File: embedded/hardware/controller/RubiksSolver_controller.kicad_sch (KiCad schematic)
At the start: 3 parts

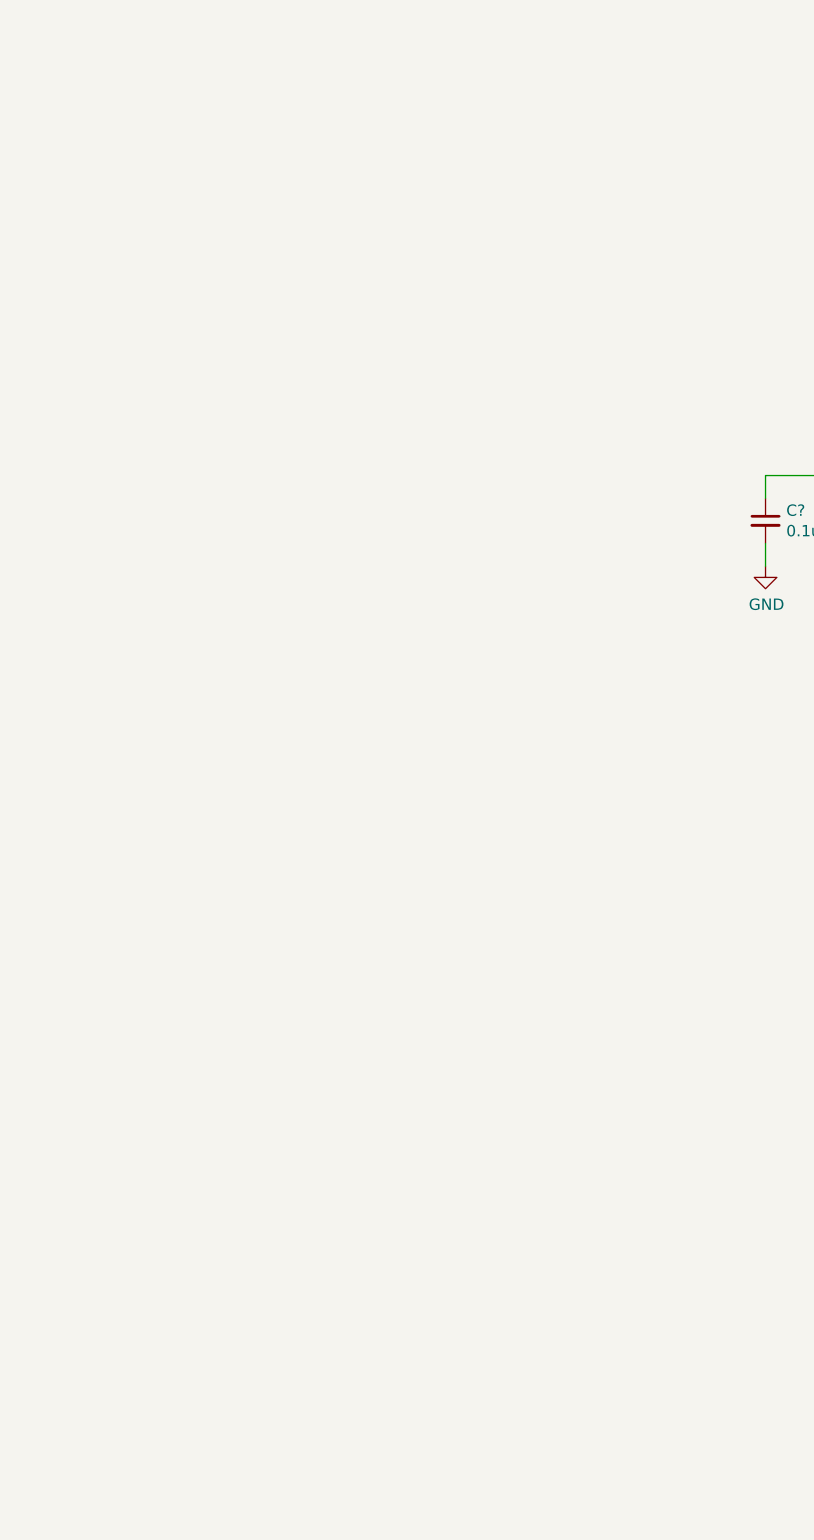
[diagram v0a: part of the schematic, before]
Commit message: Add USB Type-C receptacle
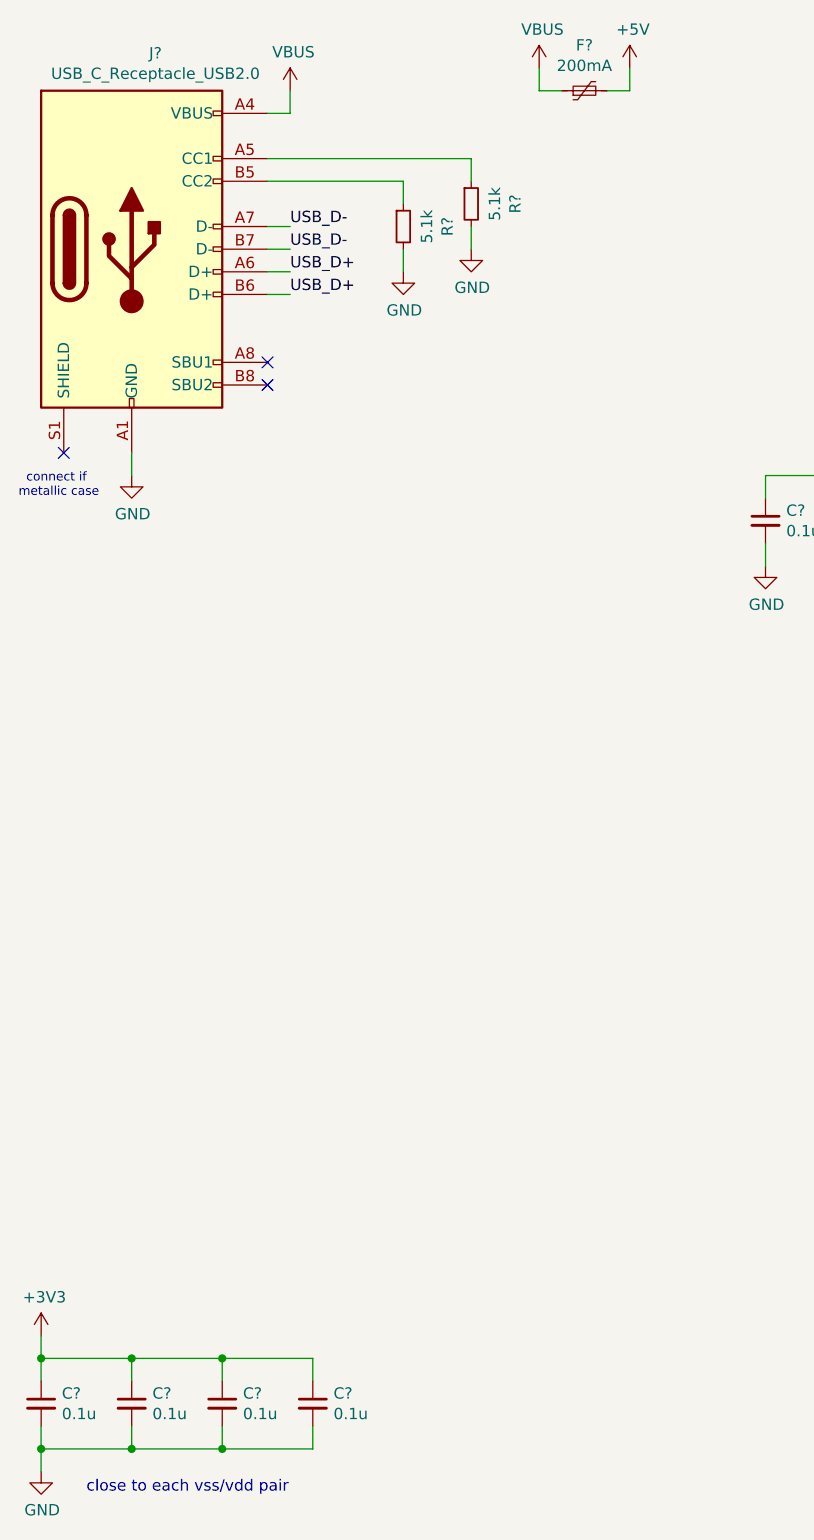
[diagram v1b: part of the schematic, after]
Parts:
- added C? (x4): 0.1u, symbol Device:C_Small
- added F?: 200mA, symbol Device:Polyfuse_Small
- added J?: USB_C_Receptacle_USB2.0, User:USB_C_Receptacle_HRO_TYPE-C-31-M-12, symbol User:USB_C_Receptacle_USB2.0
- added R? (x2): 5.1k, symbol Device:R_Small
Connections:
- net +3V3: now also C?.1, C?.1, C?.1, C?.1
- net GND: now also C?.2, C?.2, C?.2, C?.2, J?.A1 (GND), J?.A12 (GND), J?.B1 (GND), J?.B12 (GND), R?.2, R?.2
- new net: J?.A5 (CC1), R?.1
- new net: J?.B5 (CC2), R?.1
- new net +5V: F?.2
- new net USB_D+: J?.A6 (D+), J?.B6 (D+)
- new net USB_D-: J?.A7 (D-), J?.B7 (D-)
- new net VBUS: F?.1, J?.A4 (VBUS), J?.A9 (VBUS), J?.B4 (VBUS), J?.B9 (VBUS)
- no-connect marks 0 -> 3
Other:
- note added: "close to each vss/vdd pair"
- note added: "connect if metallic case"

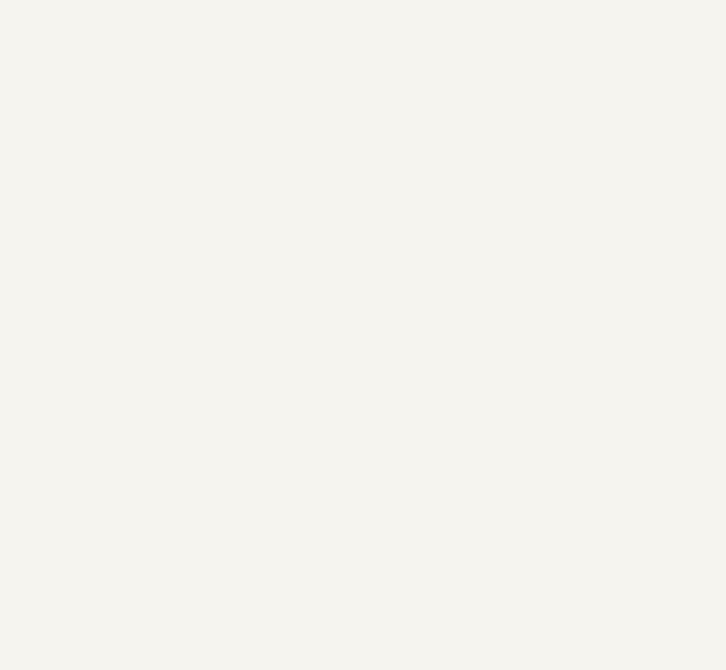
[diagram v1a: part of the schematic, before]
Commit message: Add 10pin programming header
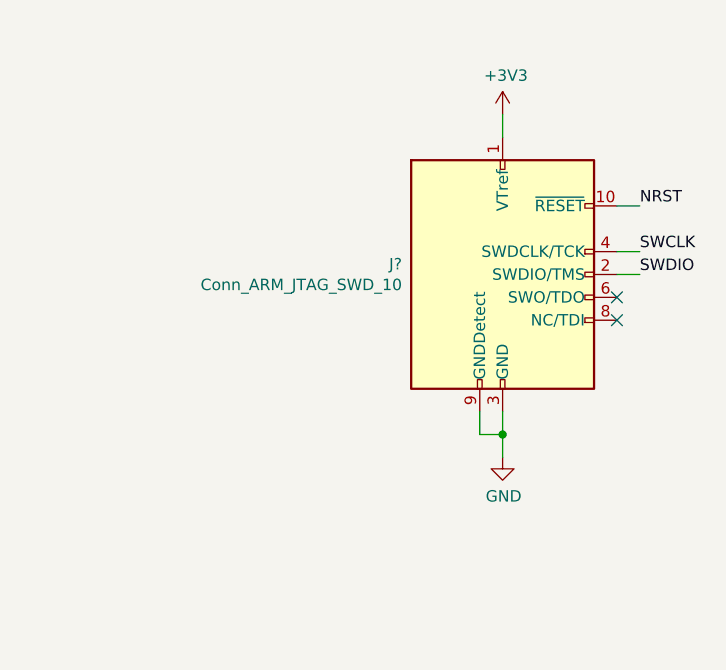
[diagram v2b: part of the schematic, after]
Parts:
- added J?: Conn_ARM_JTAG_SWD_10, symbol Connector:Conn_ARM_JTAG_SWD_10
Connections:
- net +3V3: now also J?.1 (VTref)
- net GND: now also J?.3 (GND), J?.5 (GND), J?.9 (GNDDetect)
- new net NRST: J?.10 (~RESET~)
- new net SWCLK: J?.4 (SWDCLK/TCK)
- new net SWDIO: J?.2 (SWDIO/TMS)
- no-connect marks 3 -> 5
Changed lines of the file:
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@@
   (junction (at 152.4 142.24) (diameter 0.9144) (color 0 0 0 0))
   (junction (at 154.94 60.96) (diameter 0.9144) (color 0 0 0 0))
+  (junction (at 241.3 63.5) (diameter 0.9144) (color 0 0 0 0))
   (no_connect (at 60.96 55.88))
   (no_connect (at 60.96 58.42))
+  (no_connect (at 254 48.26))
   (no_connect (at 38.1 66.04))
+  (no_connect (at 254 50.8))
   (wire (pts (xy 35.56 165.1) (xy 35.56 167.64))
     (stroke (width 0) (type solid) (color 0 0 0 0))
@@
   )
   (wire (pts (xy 157.48 60.96) (xy 157.48 63.5))
+    (stroke (width 0) (type solid) (color 0 0 0 0))
+  )
+  (wire (pts (xy 238.76 60.96) (xy 238.76 63.5))
+    (stroke (width 0) (type solid) (color 0 0 0 0))
+  )
+  (wire (pts (xy 238.76 63.5) (xy 241.3 63.5))
+    (stroke (width 0) (type solid) (color 0 0 0 0))
+  )
+  (wire (pts (xy 241.3 27.94) (xy 241.3 30.48))
+    (stroke (width 0) (type solid) (color 0 0 0 0))
+  )
+  (wire (pts (xy 241.3 60.96) (xy 241.3 63.5))
+    (stroke (width 0) (type solid) (color 0 0 0 0))
+  )
+  (wire (pts (xy 241.3 63.5) (xy 241.3 66.04))
+    (stroke (width 0) (type solid) (color 0 0 0 0))
+  )
+  (wire (pts (xy 254 38.1) (xy 256.54 38.1))
+    (stroke (width 0) (type solid) (color 0 0 0 0))
+  )
+  (wire (pts (xy 254 43.18) (xy 256.54 43.18))
+    (stroke (width 0) (type solid) (color 0 0 0 0))
+  )
+  (wire (pts (xy 254 45.72) (xy 256.54 45.72))
     (stroke (width 0) (type solid) (color 0 0 0 0))
   )
@@
     (effects (font (size 1.27 1.27)) (justify left bottom))
   )
+  (label "NRST" (at 256.54 38.1 0)
+    (effects (font (size 1.27 1.27)) (justify left bottom))
+  )
+  (label "SWCLK" (at 256.54 43.18 0)
+    (effects (font (size 1.27 1.27)) (justify left bottom))
+  )
+  (label "SWDIO" (at 256.54 45.72 0)
+    (effects (font (size 1.27 1.27)) (justify left bottom))
+  )
   (symbol (lib_id "power:+3V3") (at 35.56 165.1 0) (unit 1)
     (in_bom yes) (on_board yes)
@@
     )
   )
+  (symbol (lib_id "power:+3V3") (at 241.3 27.94 0) (unit 1)
+    (in_bom yes) (on_board yes)
+    (property "Reference" "#PWR?" (id 0) (at 241.3 31.75 0)
+      (effects (font (size 1.27 1.27)) hide)
+    )
+    (property "Value" "+3V3" (id 1) (at 241.6683 23.6156 0))
+    (property "Footprint" "" (id 2) (at 241.3 27.94 0)
+      (effects (font (size 1.27 1.27)) hide)
+    )
+    (property "Datasheet" "" (id 3) (at 241.3 27.94 0)
+      (effects (font (size 1.27 1.27)) hide)
+    )
+  )
   (symbol (lib_id "power:GND") (at 35.56 180.34 0) (unit 1)
     (in_bom yes) (on_board yes)
@@
     )
     (property "Datasheet" "" (id 3) (at 147.32 144.78 0)
+      (effects (font (size 1.27 1.27)) hide)
+    )
+  )
+  (symbol (lib_id "power:GND") (at 241.3 66.04 0) (unit 1)
+    (in_bom yes) (on_board yes)
+    (property "Reference" "#PWR?" (id 0) (at 241.3 72.39 0)
+      (effects (font (size 1.27 1.27)) hide)
+    )
+    (property "Value" "GND" (id 1) (at 241.4143 70.3644 0))
+    (property "Footprint" "" (id 2) (at 241.3 66.04 0)
+      (effects (font (size 1.27 1.27)) hide)
+    )
+    (property "Datasheet" "" (id 3) (at 241.3 66.04 0)
       (effects (font (size 1.27 1.27)) hide)
     )
@@
     )
   )
+  (symbol (lib_id "Connector:Conn_ARM_JTAG_SWD_10") (at 241.3 45.72 0) (unit 1)
+    (in_bom yes) (on_board yes)
+    (property "Reference" "J?" (id 0) (at 230.1239 44.5706 0)
+      (effects (font (size 1.27 1.27)) (justify right))
+    )
+    (property "Value" "Conn_ARM_JTAG_SWD_10" (id 1) (at 230.1239 46.8693 0)
+      (effects (font (size 1.27 1.27)) (justify right))
+    )
+    (property "Footprint" "" (id 2) (at 241.3 45.72 0)
+      (effects (font (size 1.27 1.27)) hide)
+    )
+    (property "Datasheet" "http://infocenter.arm.com/help/topic/com.arm.doc.ddi0314h/DDI0314H_coresight_components_trm.pdf" (id 3) (at 232.41 77.47 90)
+      (effects (font (size 1.27 1.27)) hide)
+    )
+  )
   (symbol (lib_id "User:USB_C_Receptacle_USB2.0") (at 45.72 43.18 0) (unit 1)
     (in_bom yes) (on_board yes)
@@
   )
   (symbol_instances
+    (path "/259b77ed-a074-4b54-8027-04ba979215be"
+      (reference "#PWR?") (unit 1) (value "GND") (footprint "")
+    )
     (path "/2a143cb8-a1de-4742-8f35-f2f7b31e5171"
       (reference "#PWR?") (unit 1) (value "GND") (footprint "")
@@
       (reference "#PWR?") (unit 1) (value "+5V") (footprint "")
     )
+    (path "/6128e785-f6ee-489b-8337-ca8a83111c1b"
+      (reference "#PWR?") (unit 1) (value "+3V3") (footprint "")
+    )
     (path "/64c8ed70-14a8-4a73-98d8-e686a93ff02b"
       (reference "#PWR?") (unit 1) (value "+3V3") (footprint "")
@@
       (reference "F?") (unit 1) (value "200mA") (footprint "")
     )
+    (path "/1b09b775-5ad9-4d5e-b556-9eea678e2fda"
+      (reference "J?") (unit 1) (value "Conn_ARM_JTAG_SWD_10") (footprint "")
+    )
     (path "/21b2b0fd-3066-40b4-9516-728461709173"

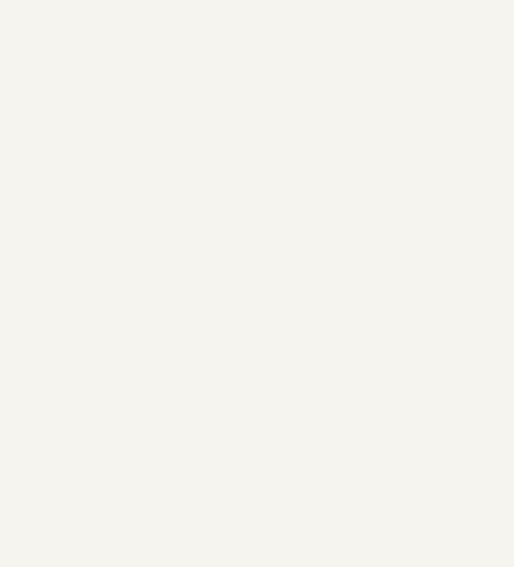
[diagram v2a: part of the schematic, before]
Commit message: Add 4x mounting holes
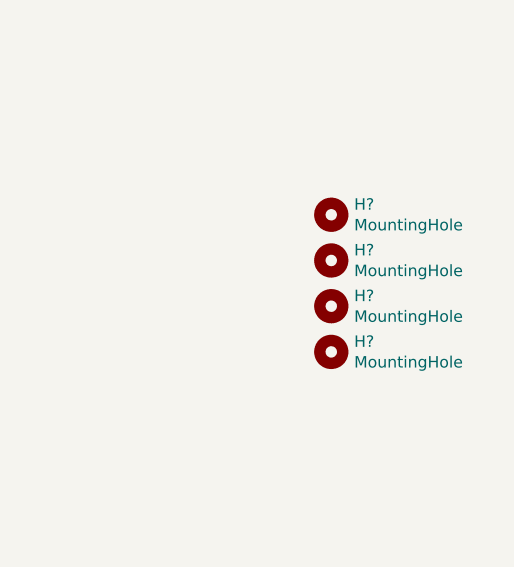
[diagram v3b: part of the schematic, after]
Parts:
- added H? (x4): MountingHole, symbol Mechanical:MountingHole
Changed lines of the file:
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@@
+    )
+  )
+  (symbol (lib_id "Mechanical:MountingHole") (at 256.54 139.7 0) (unit 1)
+    (in_bom yes) (on_board yes)
+    (property "Reference" "H?" (id 0) (at 259.0801 138.5506 0)
+      (effects (font (size 1.27 1.27)) (justify left))
+    )
+    (property "Value" "MountingHole" (id 1) (at 259.0801 140.8493 0)
+      (effects (font (size 1.27 1.27)) (justify left))
+    )
+    (property "Footprint" "" (id 2) (at 256.54 139.7 0)
+      (effects (font (size 1.27 1.27)) hide)
+    )
+    (property "Datasheet" "~" (id 3) (at 256.54 139.7 0)
+      (effects (font (size 1.27 1.27)) hide)
+    )
+  )
+  (symbol (lib_id "Mechanical:MountingHole") (at 256.54 144.78 0) (unit 1)
+    (in_bom yes) (on_board yes)
+    (property "Reference" "H?" (id 0) (at 259.0801 143.6306 0)
+      (effects (font (size 1.27 1.27)) (justify left))
+    )
+    (property "Value" "MountingHole" (id 1) (at 259.0801 145.9293 0)
+      (effects (font (size 1.27 1.27)) (justify left))
+    )
+    (property "Footprint" "" (id 2) (at 256.54 144.78 0)
+      (effects (font (size 1.27 1.27)) hide)
+    )
+    (property "Datasheet" "~" (id 3) (at 256.54 144.78 0)
+      (effects (font (size 1.27 1.27)) hide)
+    )
+  )
+  (symbol (lib_id "Mechanical:MountingHole") (at 256.54 149.86 0) (unit 1)
+    (in_bom yes) (on_board yes)
+    (property "Reference" "H?" (id 0) (at 259.0801 148.7106 0)
+      (effects (font (size 1.27 1.27)) (justify left))
+    )
+    (property "Value" "MountingHole" (id 1) (at 259.0801 151.0093 0)
+      (effects (font (size 1.27 1.27)) (justify left))
+    )
+    (property "Footprint" "" (id 2) (at 256.54 149.86 0)
+      (effects (font (size 1.27 1.27)) hide)
+    )
+    (property "Datasheet" "~" (id 3) (at 256.54 149.86 0)
+      (effects (font (size 1.27 1.27)) hide)
+    )
+  )
+  (symbol (lib_id "Mechanical:MountingHole") (at 256.54 154.94 0) (unit 1)
+    (in_bom yes) (on_board yes)
+    (property "Reference" "H?" (id 0) (at 259.0801 153.7906 0)
+      (effects (font (size 1.27 1.27)) (justify left))
+    )
+    (property "Value" "MountingHole" (id 1) (at 259.0801 156.0893 0)
+      (effects (font (size 1.27 1.27)) (justify left))
+    )
+    (property "Footprint" "" (id 2) (at 256.54 154.94 0)
+      (effects (font (size 1.27 1.27)) hide)
+    )
+    (property "Datasheet" "~" (id 3) (at 256.54 154.94 0)
+      (effects (font (size 1.27 1.27)) hide)
     )
   )
@@
       (reference "F?") (unit 1) (value "200mA") (footprint "")
     )
+    (path "/5255a4cf-5584-4418-ae36-756d1cdb87fd"
+      (reference "H?") (unit 1) (value "MountingHole") (footprint "")
+    )
+    (path "/595895bc-98c8-4dfa-8bb7-90db10c1d5b7"
+      (reference "H?") (unit 1) (value "MountingHole") (footprint "")
+    )
+    (path "/62c0e475-a278-400f-a8ae-cbb207ba5533"
+      (reference "H?") (unit 1) (value "MountingHole") (footprint "")
+    )
+    (path "/b67c8cfb-dbab-44ff-8c58-a653c94d0f11"
+      (reference "H?") (unit 1) (value "MountingHole") (footprint "")
+    )
     (path "/1b09b775-5ad9-4d5e-b556-9eea678e2fda"
